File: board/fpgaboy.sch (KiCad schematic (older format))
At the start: 53 parts, among them P1 CONN_01X02, P2 ILI9341, Q1 BSS816NW, SW1 SWITCH_SPST, U1 iCE40-HX8K-CT256, U2 NCP1532, U3 BQ21040, U4 GS74116AGP/, U5 FT2232H

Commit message: Add flash, eeprom and oscillator to schematic. Add some footprints
Former-commit-id: 7ac2ef4c4fae7cdb8e0b55eb8623fde80e732552
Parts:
- added C23: 10u, Capacitors_SMD:C_0805, symbol C
- added C24, C25, C?: 0.1u, Capacitors_SMD:C_0603, symbol C
- added P3: USB_OTG, fpgaboy_parts:USB_Micro-B, symbol USB_OTG
- added R19: NF, Resistors_SMD:R_0603, symbol R
- added R20, R21, R22, R23, R25, R26, R27: 10k, Resistors_SMD:R_0603, symbol R
- added R24: 2k2, Resistors_SMD:R_0603, symbol R
- added U6: 93LC56B, SMD_Packages:SOIC-8-N, symbol 93LC56B
- added U7: S25FL132K, SMD_Packages:SOIC-8-N, symbol S25FL132K
- added U?: DSC60XX, symbol DSC60XX
- SW1: footprint (none) -> fpgaboy_parts:SPDT_SLIDE_SWITCH
- TP1: footprint (none) -> fpgaboy_parts:tiepoint-0.5
- U5: footprint (none) -> fpgaboy_parts:QFN_64_0.5mm
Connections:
- net labels added: FLASH_CS, FLASH_MISO, FLASH_MOSI, FLASH_SCK, UART_CTS, UART_DCD, UART_DSR, UART_DTR, UART_RTS, UART_RX, UART_TX, iCE_CDONE, iCE_CREST
- wire segments 275 -> 446
- no-connect marks 7 -> 30
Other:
- note added: "12MHz MEMS oscillator"
- moved on the sheet: C10, C11, C16, C17, C18, C19, C20, C21, C22, C8, C9, R15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

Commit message: Correct bug in opcode list parsing. Remove non-RV32IC opcodes from header.
Former-commit-id: 397b3a49cdce0db2d0dabde518f7a9a4f9154396
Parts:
- U8: renamed from U?; footprint (none) -> fpgaboy_parts:LGA4_1.6x1.2mm
- gave numbers to parts that had none: 1
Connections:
- wire segments 446 -> 372

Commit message: Chasing busfabric bugs.
Former-commit-id: c45fde4014cf416347e1dc4e27e6da2cc6d71206
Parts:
- added P?: CONN_01X12, symbol CONN_01X12
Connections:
- net labels added: GPIO_SW0, GPIO_SW1, GPIO_SW2, GPIO_SW3, GPIO_SW4, GPIO_SW5, GPIO_SW6, GPIO_SW7, GPIO_SW8, GPIO_SW9
- wire segments 372 -> 395
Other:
- note added: "Buttons"
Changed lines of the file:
@@
 Text Notes 4900 6950 0    60   ~ 0
 12MHz MEMS oscillator
+Text Notes 6300 8700 0    60   ~ 0
+Buttons
+$Comp
+L CONN_01X12 P?
+U 1 1 5A92DF3A
+P 6500 9450
+F 0 "P?" H 6500 10100 50  0000 C CNN
+F 1 "CONN_01X12" V 6600 9450 50  0000 C CNN
+F 2 "" H 6500 9450 50  0000 C CNN
+F 3 "" H 6500 9450 50  0000 C CNN
+	1    6500 9450
+	1    0    0    -1
+$EndComp
+Wire Wire Line
+	6300 8900 6200 8900
+Wire Wire Line
+	6200 8900 6200 10100
+Wire Wire Line
+	6300 10000 6200 10000
+Connection ~ 6200 10000
+$Comp
+L GND #PWR?
+U 1 1 5A92E42C
+P 6200 10100
+F 0 "#PWR?" H 6200 9850 50  0001 C CNN
+F 1 "GND" H 6200 9950 50  0000 C CNN
+F 2 "" H 6200 10100 50  0000 C CNN
+F 3 "" H 6200 10100 50  0000 C CNN
+	1    6200 10100
+	1    0    0    -1
+$EndComp
+Wire Wire Line
+	6300 9000 6100 9000
+Wire Wire Line
+	6300 9100 6100 9100
+Wire Wire Line
+	6300 9200 6100 9200
+Wire Wire Line
+	6300 9300 6100 9300
+Wire Wire Line
+	6300 9400 6100 9400
+Wire Wire Line
+	6300 9500 6100 9500
+Wire Wire Line
+	6300 9600 6100 9600
+Wire Wire Line
+	6300 9700 6100 9700
+Wire Wire Line
+	6300 9800 6100 9800
+Wire Wire Line
+	6300 9900 6100 9900
+Text Label 6100 9000 2    60   ~ 0
+GPIO_SW0
+Text Label 6100 9100 2    60   ~ 0
+GPIO_SW1
+Text Label 6100 9200 2    60   ~ 0
+GPIO_SW2
+Text Label 6100 9300 2    60   ~ 0
+GPIO_SW3
+Text Label 6100 9400 2    60   ~ 0
+GPIO_SW4
+Text Label 6100 9500 2    60   ~ 0
+GPIO_SW5
+Text Label 6100 9600 2    60   ~ 0
+GPIO_SW6
+Text Label 6100 9700 2    60   ~ 0
+GPIO_SW7
+Text Label 6100 9800 2    60   ~ 0
+GPIO_SW8
+Text Label 6100 9900 2    60   ~ 0
+GPIO_SW9
+Text Label 4500 1400 2    60   ~ 0
+GPIO_SW0
+Wire Wire Line
+	4600 1400 4500 1400
+Wire Wire Line
+	4600 1500 4500 1500
+Wire Wire Line
+	4600 1600 4500 1600
+Wire Wire Line
+	4600 1700 4500 1700
+Wire Wire Line
+	4600 1800 4500 1800
+Wire Wire Line
+	4600 1900 4500 1900
+Wire Wire Line
+	4600 2000 4500 2000
+Wire Wire Line
+	4600 2100 4500 2100
+Wire Wire Line
+	4600 2200 4500 2200
+Wire Wire Line
+	4600 2300 4500 2300
+Text Label 4500 1500 2    60   ~ 0
+GPIO_SW1
+Text Label 4500 1600 2    60   ~ 0
+GPIO_SW2
+Text Label 4500 1700 2    60   ~ 0
+GPIO_SW3
+Text Label 4500 1800 2    60   ~ 0
+GPIO_SW4
+Text Label 4500 1900 2    60   ~ 0
+GPIO_SW5
+Text Label 4500 2000 2    60   ~ 0
+GPIO_SW6
+Text Label 4500 2100 2    60   ~ 0
+GPIO_SW7
+Text Label 4500 2300 2    60   ~ 0
+GPIO_SW9
+Text Label 4500 2200 2    60   ~ 0
+GPIO_SW8
 $EndSCHEMATC

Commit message: Create BG121 symbol for iCE40. Mostly wire this up. New kicad version has moved some files around.
Former-commit-id: e45c33045238516c7f00d15ed939b18139a34b1a
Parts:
- removed C10, C11, C8, C9: 0.1u, Capacitors_SMD:C_0603, symbol C
- removed C7: 1u, Capacitors_SMD:C_0603, symbol C
- removed R9: 100, Resistors_SMD:R_0603, symbol R
- removed U1: iCE40-HX8K-CT256, fpgaboy_parts:BGA_256_0.8mm, symbol iCE40-HX8K-CT256
- added C? (x2): 1u, Capacitors_SMD:C_0603, symbol fpgaboy-rescue:C
- added R? (x2): 10, Resistors_SMD:R_0603, symbol fpgaboy-rescue:R
- added U? (x6): iCE40-HX8k-BG121, symbol fpgaboy_parts:iCE40-HX8k-BG121
- C1, C12, C13, C14, C15, C16, C17, C18, C19, C2, C20, C21, C22, C23, C24, C25, C26, C3, C4, C5, C6: symbol C -> fpgaboy-rescue:C
- D1: symbol LED -> fpgaboy-rescue:LED
- L1, L2: symbol L -> fpgaboy-rescue:L
- P1: symbol CONN_01X02 -> fpgaboy-rescue:CONN_01X02
- P2: symbol ILI9341 -> fpgaboy-rescue:ILI9341
- P3: symbol USB_OTG -> fpgaboy-rescue:USB_OTG
- P?: symbol CONN_01X12 -> fpgaboy-rescue:CONN_01X12
- Q1: symbol Q_NMOS_GSD -> fpgaboy-rescue:Q_NMOS_GSD
- R1, R10, R11, R12, R13, R14, R15, R16, R17, R18, R19, R2, R20, R21, R22, R23, R24, R25, R26, R27, R3, R4, R5, R6, R7, R8: symbol R -> fpgaboy-rescue:R
- SW1: symbol SWITCH_SPST -> fpgaboy-rescue:SWITCH_SPST
- TP1: symbol Tie_point -> fpgaboy-rescue:Tie_point
- U2: symbol NCP1532 -> fpgaboy-rescue:NCP1532
- U3: symbol BQ21040 -> fpgaboy-rescue:BQ21040
- U4: symbol GS74116AGP/ -> fpgaboy-rescue:GS74116AGP_
- U5: symbol FT2232H -> fpgaboy-rescue:FT2232H
- U6: symbol 93LC56B -> fpgaboy-rescue:93LC56B
- U7: symbol S25FL132K -> fpgaboy-rescue:S25FL132K
- U8: symbol DSC60XX -> fpgaboy-rescue:DSC60XX
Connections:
- wire segments 395 -> 466
- no-connect marks 30 -> 29
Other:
- note added: "FPGA"
- moved on the sheet: C26, U8

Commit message: Update FPGA config circuitry in schematic
Former-commit-id: d9e5c3010d90954b8d868f76662156070ad66b1c
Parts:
- added C10, C11, C13, C14, C23, C5, C6, C7, C8: 0.1u, Capacitors_SMD:C_0603, symbol fpgaboy-rescue:C
- added C33, C34: 1u, Capacitors_SMD:C_0603, symbol fpgaboy-rescue:C
- added J1: Micro_SD_Card, symbol Connector:Micro_SD_Card
- added TP1, TP2, TP3, TP4, TP5, TP6, TP7: TestPoint, symbol Connector:TestPoint
- gave numbers to parts that had none: 6
- renumbered C12 to C1, C15 to C12, C23 to C15, C13 to C2, C1 to C24, C24 to C27, C2 to C28, C3 to C29, C4 to C30, C5 to C31, C6 to C32, C14 to C9, P2 to P1, P1 to P4, R10 to R1, R15 to R10, R17 to R11, R1 to R12, R18 to R13, R20 to R14, R21 to R15, R2 to R16, R3 to R17, R4 to R18, R5 to R19, R11 to R2, R22 to R20, R26 to R21, R23 to R22, R24 to R23, R27 to R24, R6 to R26, R7 to R27, R8 to R28, R12 to R3, R13 to R4, R14 to R5, R16 to R8, R19 to R9, TP1 to TP8, U4 to U2, U5 to U3, U2 to U4, U8 to U5, U3 to U8
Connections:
- net +1V2: now also R6.2, R7.2, C11.1, C14.1, C34.1, C6.1, C8.1, TP5.1
- net +3V3: now also U1.D6 (VCCIO_0), U1.F8 (VCCIO_1), U1.H6 (VCCIO_2), U1.L11 (VCC_SPI), U2.11 (VDD), C10.1, C13.1, C23.1, C33.1, C5.1, C7.1, J1.4 (VDD), TP6.1; no longer R6.2, R7.2, U1.B10 (VPP_FAST)
- net CLK_OSC: now also U1.L5 (IOB_81_GBIN5)
- net FT_EECS: now also R25.2; no longer R20.2
- net FT_EEDATA: no longer R25.2
- net GND: now also C10.2, C11.2, C13.2, C14.2, C23.2, C33.2, C34.2, C5.2, C6.2, C7.2, C8.2, J1.6 (VSS), J1.9 (SHIELD), TP7.1
- net GPIO_SW0: now also U1.A6 (IOT_206); no longer U1.H10 (IOR_116)
- net GPIO_SW1: now also U1.A5 (IOT_207); no longer U1.J10 (IOR_117)
- net GPIO_SW2: now also U1.B5 (IOT_208); no longer U1.G8 (IOR_118)
- net GPIO_SW3: now also U1.A4 (IOT_211); no longer U1.H11 (IOR_119)
- net GPIO_SW4: now also U1.D5 (IOT_212); no longer U1.G10 (IOR_120)
- net GPIO_SW5: now also U1.B4 (IOT_219); no longer U1.G9 (IOR_128)
- net GPIO_SW6: now also U1.B3 (IOT_221); no longer U1.G11 (IOR_129)
- net GPIO_SW7: now also U1.A2 (IOT_222); no longer U1.F10 (IOR_136)
- net GPIO_SW8: now also U1.A3 (IOT_223); no longer U1.F9 (IOR_137)
- net GPIO_SW9: now also U1.A1 (IOT_225); no longer U1.E9 (IOR_144)
- net LCD_CS: now also TP3.1
- net LCD_D/C: now also TP2.1
- net LCD_SDA: now also TP4.1
- net at R23.2, U6.4 (SDO): now also R20.2
- net LCD_SDL renamed LCD_SCL
- net LCD_SCL: now also TP1.1; no longer P1.7 (SDO), U1.B11 (IOR_161)
- new net LCD_SDO: P1.7 (SDO), U1.B11 (IOR_161)
- new net uSD_CLK: J1.5 (CLK), U1.G9 (IOR_128)
- new net uSD_CMD: J1.3 (CMD), U1.G10 (IOR_120)
- new net uSD_DAT0: J1.7 (DAT0), U1.H10 (IOR_116)
- new net uSD_DAT1: J1.8 (DAT1), U1.J10 (IOR_117)
- new net uSD_DAT2: J1.1 (DAT2), U1.G8 (IOR_118)
- new net uSD_DAT3: J1.2 (DAT3/CD), U1.H11 (IOR_119)
- no-connect marks 29 -> 61
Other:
- note added: "F2232H Config"
- note added: "FPGA Config"
- note added: "FPGA decoupling"
- moved on the sheet: C12, C15, C16, C17, C18, C19, C20, C21, C22, C25, C26, C27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

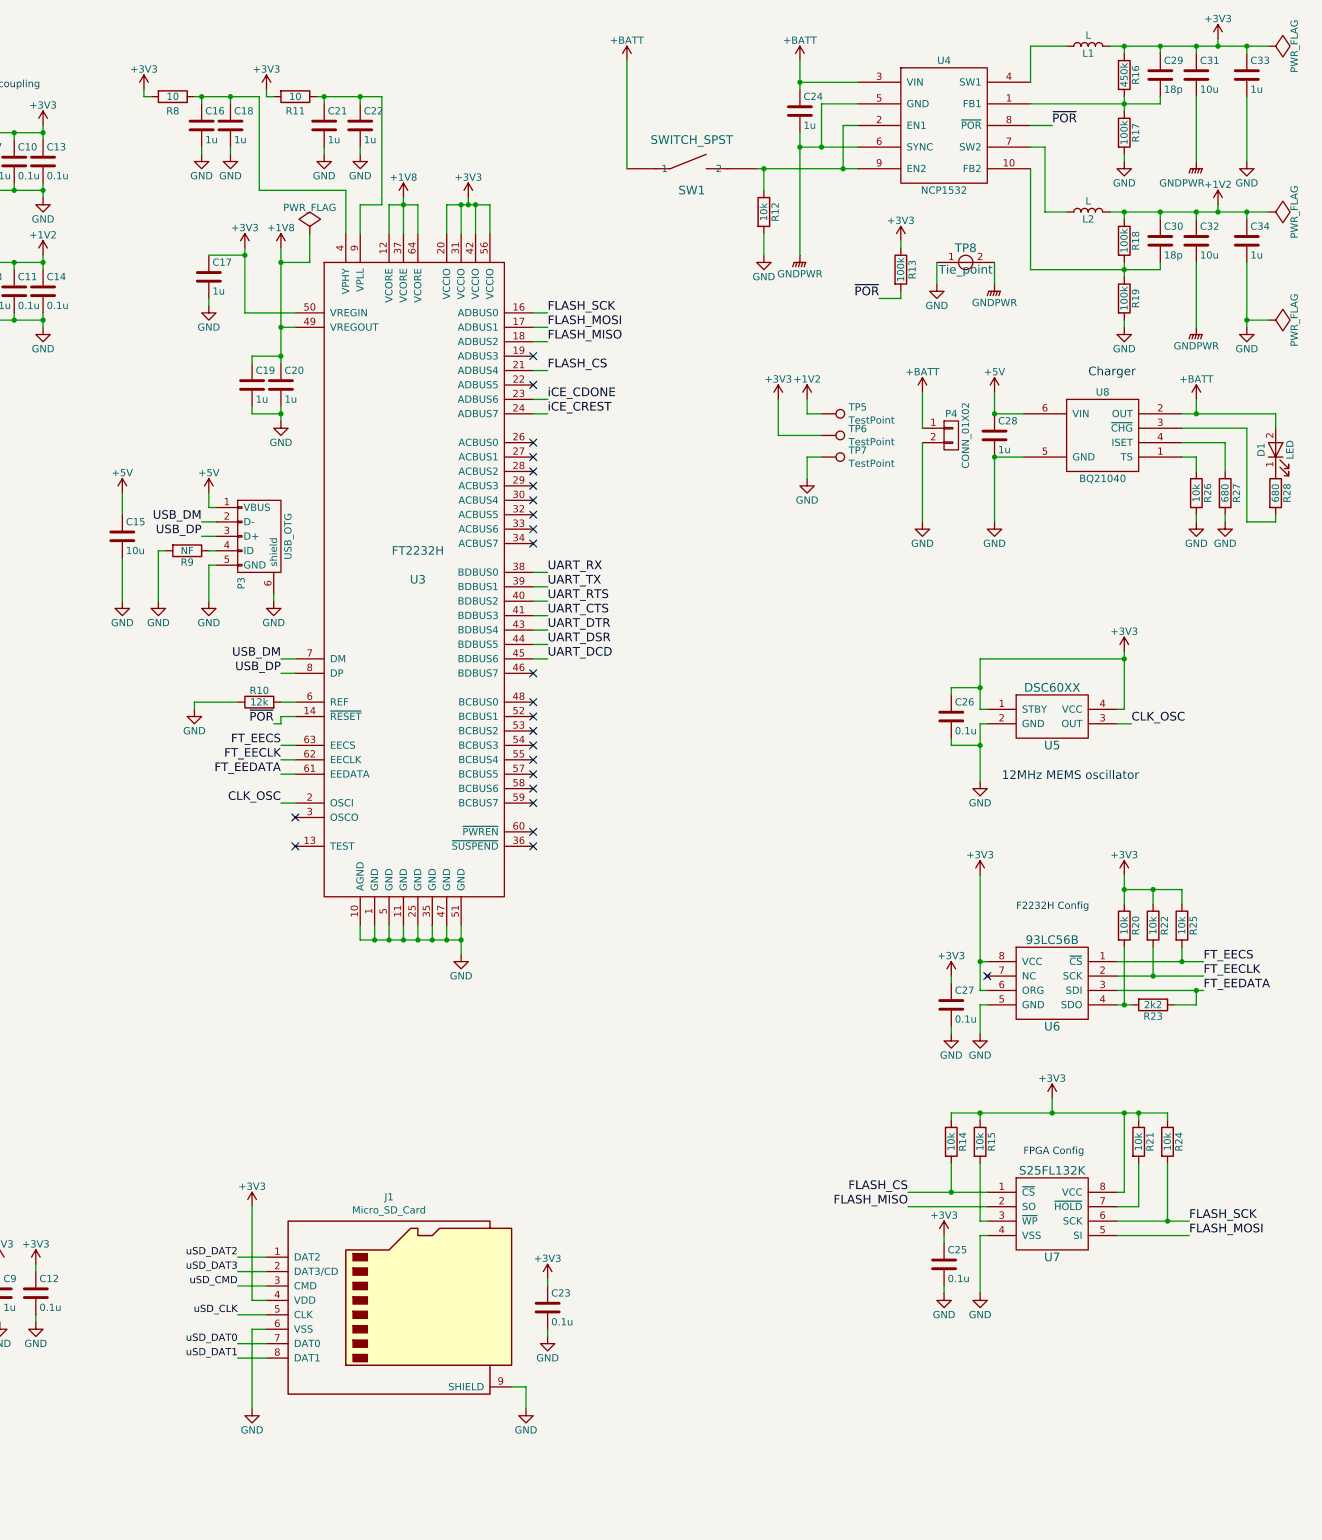
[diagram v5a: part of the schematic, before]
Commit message: Schematic: remove FT2232H. Add debug connector. Add datasheet for a better microcontroller.
Former-commit-id: 58bdfe8228768011608435203ff3ba7e6b664fb3 [formerly 19c51b7f48ccd36d2be7f46b66d55bb2d971f80c]
Former-commit-id: a48f46e7092b9bd3871c3da2e30a9efbadde95d5
Former-commit-id: 433e187ffcc20f4383464b4435a475bd7f0d864e
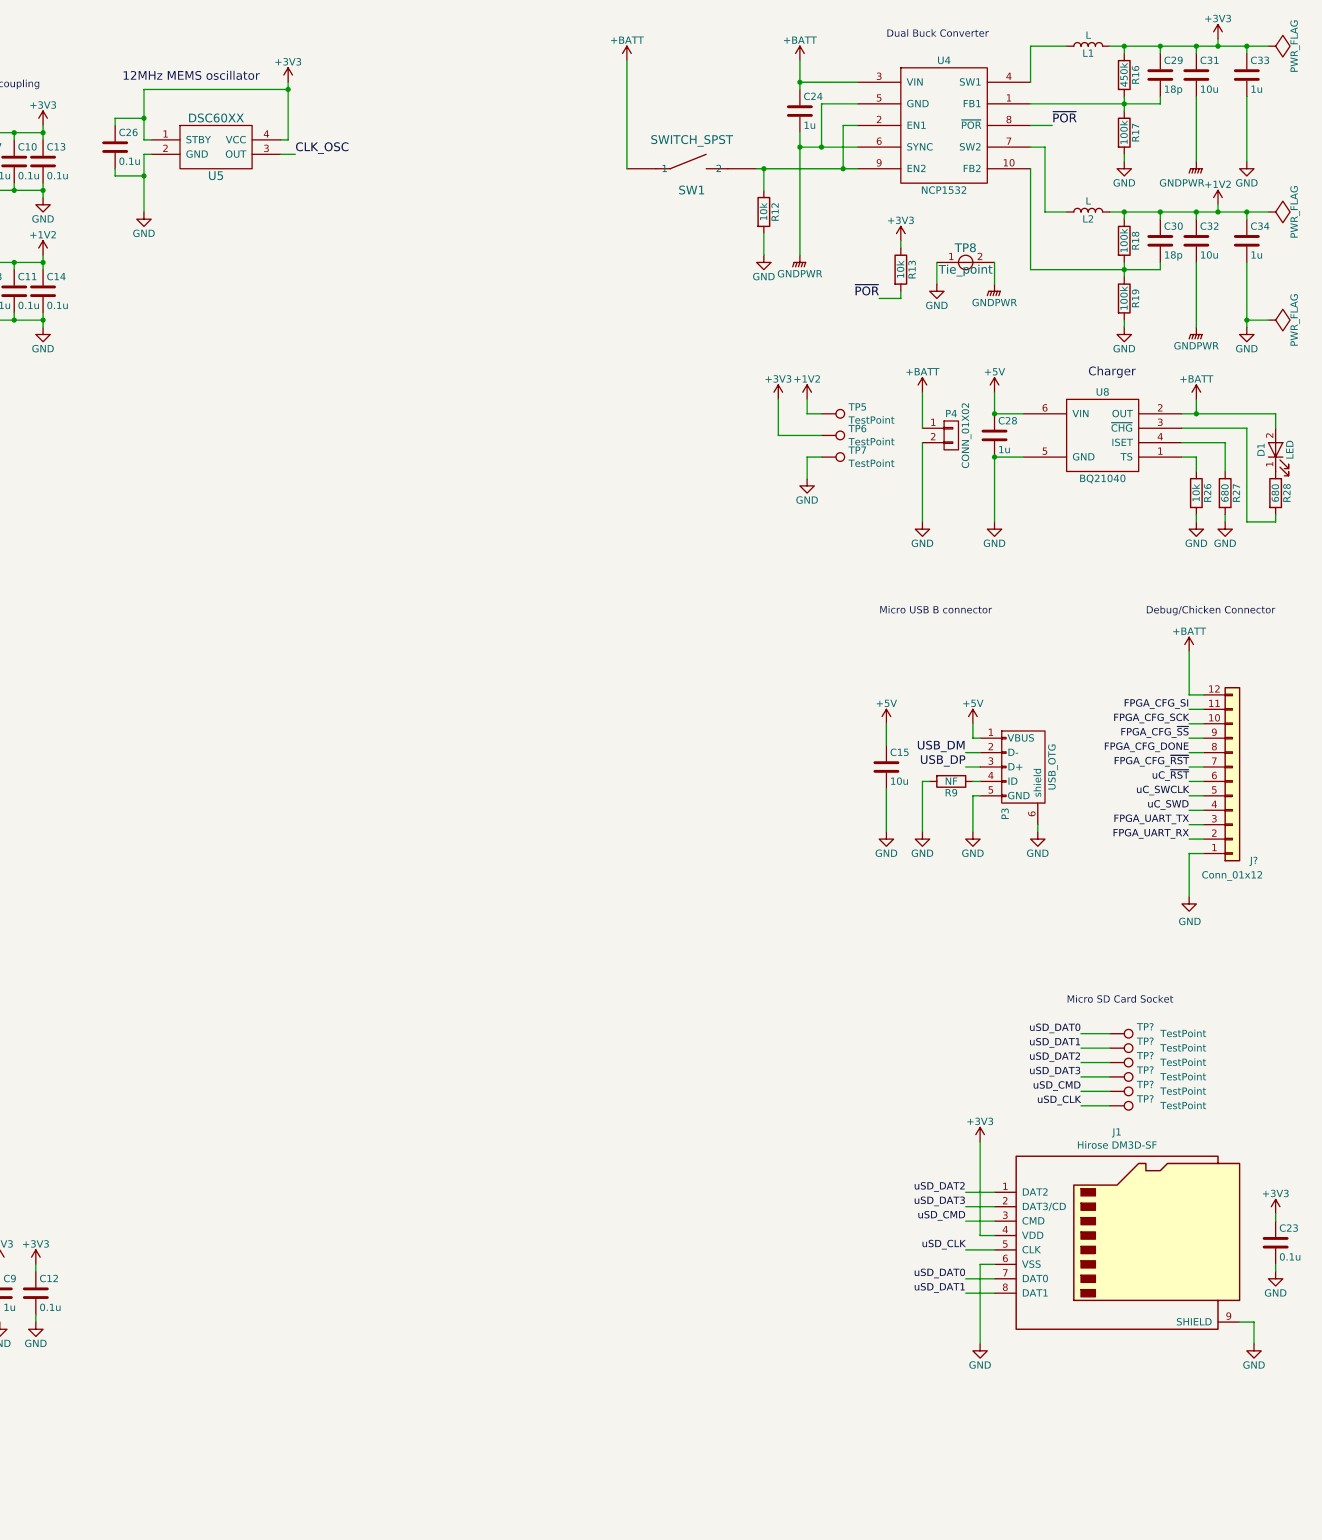
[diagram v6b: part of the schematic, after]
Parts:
- removed C16, C17, C18, C19, C20, C21, C22: 1u, Capacitors_SMD:C_0603, symbol fpgaboy-rescue:C
- removed C25, C27: 0.1u, Capacitors_SMD:C_0603, symbol fpgaboy-rescue:C
- removed R10: 12k, Resistors_SMD:R_0603, symbol fpgaboy-rescue:R
- removed R11, R8: 10, Resistors_SMD:R_0603, symbol fpgaboy-rescue:R
- removed R14, R15, R20, R21, R22, R24, R25: 10k, Resistors_SMD:R_0603, symbol fpgaboy-rescue:R
- removed R23: 2k2, Resistors_SMD:R_0603, symbol fpgaboy-rescue:R
- removed U3: FT2232H, fpgaboy_parts:QFN_64_0.5mm, symbol fpgaboy-rescue:FT2232H
- removed U6: 93LC56B, SMD_Packages:SOIC-8-N, symbol fpgaboy-rescue:93LC56B
- removed U7: S25FL132K, SMD_Packages:SOIC-8-N, symbol fpgaboy-rescue:S25FL132K
- added J?: Conn_01x12, symbol Connector_Generic:Conn_01x12
- added TP? (x6): TestPoint, symbol Connector:TestPoint
- J1: value Micro_SD_Card -> Hirose DM3D-SF
- R13: value 100k -> 10k
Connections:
- net +BATT: now also J?.12 (Pin_12)
- net GND: now also J?.1 (Pin_1)
- net uSD_CLK: now also TP?.1
- net uSD_CMD: now also TP?.1
- net uSD_DAT0: now also TP?.1
- net uSD_DAT1: now also TP?.1
- net uSD_DAT2: now also TP?.1
- net uSD_DAT3: now also TP?.1
- new net FPGA_CFG_DONE: J?.8 (Pin_8)
- new net FPGA_CFG_SCK: J?.10 (Pin_10)
- new net FPGA_CFG_SI: J?.11 (Pin_11)
- new net FPGA_CFG_~RST: J?.7 (Pin_7)
- new net FPGA_CFG_~SS: J?.9 (Pin_9)
- new net FPGA_UART_RX: J?.2 (Pin_2)
- new net FPGA_UART_TX: J?.3 (Pin_3)
- new net uC_SWCLK: J?.5 (Pin_5)
- new net uC_SWD: J?.4 (Pin_4)
- new net uC_~RST: J?.6 (Pin_6)
- no-connect marks 61 -> 37
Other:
- note added: "Debug/Chicken Connector\n"
- note added: "Dual Buck Converter\n"
- note added: "Micro SD Card Socket\n"
- note added: "Micro USB B connector\n"
- note removed: "F2232H Config"
- note removed: "FPGA Config"
- moved on the sheet: C15, C23, C26, J1, P3, R9, U5

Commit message: Update TODO after ATXMEGA boot investigation. Small schematic updates. Specify a power inductor for buck converters.
Former-commit-id: 586be8256e79858f7111731a34fe6ef163739060 [formerly 97448644a8469dd8cefe4e310b3627ed06cd7808]
Former-commit-id: 3bf18d91c30ecc2b96a7fe993086419bc1b087ca
Former-commit-id: c2c9c4b26ce43b5d69dd4ad5f325b8a792337350
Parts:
- L1, L2: value L -> 2u2
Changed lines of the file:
@@
 P 14550 700
 F 0 "L1" V 14500 700 50  0000 C CNN
-F 1 "L" V 14625 700 50  0000 C CNN
+F 1 "2u2" V 14625 700 50  0000 C CNN
 F 2 "Resistors_SMD:R_0805" H 14550 700 50  0001 C CNN
 F 3 "" H 14550 700 50  0000 C CNN
@@
 P 14550 1850
 F 0 "L2" V 14500 1850 50  0000 C CNN
-F 1 "L" V 14625 1850 50  0000 C CNN
+F 1 "2u2" V 14625 1850 50  0000 C CNN
 F 2 "Resistors_SMD:R_0805" H 14550 1850 50  0001 C CNN
 F 3 "" H 14550 1850 50  0000 C CNN

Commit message: Create symbol for SAML22G18A, and wire up its reset + power in schematic.
Former-commit-id: f8500376bb14c4c390649148718081ca3b6a35f1 [formerly 521bb755447660a73386e8553a6c7468d998e60e]
Former-commit-id: 26e2e9ec17376e09dd901902dce13d3365899e41
Former-commit-id: fe970733337899ed4e4bdd0aab35c62028279936
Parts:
- removed R13: 10k, Resistors_SMD:R_0603, symbol fpgaboy-rescue:R
- added C? (x2): 100n, symbol Device:C_Small
- added C?: 1u, symbol Device:C_Small
- added R? (x3): 10k, symbol Device:R_Small
- added U?: SAML22G18A, symbol fpgaboy_parts:SAML22G18A
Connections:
- net ~POR is gone; now on net uC_~RST: U4.8 (~POR)
- net +3V3: now also C?.1, R?.1, R?.1, R?.1, U?.17 (VDDIO), U?.19 (VLCD), U?.36 (VDDIO), U?.44 (VDDIO), U?.6 (VDDANA)
- net GND: now also C?.2, C?.2, C?.2, U?.18 (GND), U?.35 (GND), U?.42 (GNDANA), U?.5 (GND)
- net uC_SWCLK: now also R?.2, U?.45 (PA30/SWCLK)
- net uC_SWD: now also R?.2, U?.46 (PA31/SWDIO)
- net uC_~RST: now also R?.2, U?.40 (~RST)
- new net VDDCORE: C?.1, C?.1, U?.41 (VDDCORE)
- no-connect marks 37 -> 38
